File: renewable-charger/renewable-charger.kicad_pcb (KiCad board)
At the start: 0 parts

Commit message: Schematic almost finished—most components chosen with part numbers.  Start made on PCB.  Part of #2
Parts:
- added BT1: Battery_Cell, Connector_JST:JST_PH_S2B-PH-SM4-TB_1x02-1MP_P2.00mm_Horizontal, F.Cu at (158.8, 71.1)
- added C1: 1uF, Capacitor_SMD:C_0603_1608Metric_Pad1.08x0.95mm_HandSolder, F.Cu at (142.9, 73.7)
- added C2: 0.1uF, Capacitor_SMD:C_0603_1608Metric_Pad1.08x0.95mm_HandSolder, F.Cu at (75.6, 89.5)
- added C3: 1uF, Capacitor_SMD:C_0603_1608Metric_Pad1.08x0.95mm_HandSolder, F.Cu at (99.7, 69.2)
- added C4: 220nF, Capacitor_SMD:C_0603_1608Metric_Pad1.08x0.95mm_HandSolder, F.Cu at (137.2, 83.2)
- added C6: 10uF 50V, Capacitor_SMD:C_1206_3216Metric_Pad1.33x1.80mm_HandSolder, F.Cu at (92.1, 59.7)
- added C7: 10uF 50V, Capacitor_SMD:C_1206_3216Metric_Pad1.33x1.80mm_HandSolder, F.Cu at (99.7, 65.4)
- added D1: D_Zener, Diode_SMD:D_SMF, F.Cu at (114.9, 48.9)
- added D2: D_Zener, Diode_SMD:D_SMF, F.Cu at (106.7, 48.9)
- added D3: LED Green, LED_SMD:LED_0805_2012Metric_Pad1.15x1.40mm_HandSolder, F.Cu at (64.8, 76.8)
- added D4: LED Red, LED_SMD:LED_0805_2012Metric_Pad1.15x1.40mm_HandSolder, F.Cu at (64.8, 71.1)
- added L1: 100uH 2.5A, Inductor_SMD:L_12x12mm_H6mm, F.Cu at (74.3, 54.0)
- added Q1: P-channel 30V 4A MOSfet, Package_TO_SOT_SMD:SOT-23, F.Cu at (124.5, 52.1)
- added R1: R_Small, Resistor_SMD:R_0603_1608Metric_Pad0.98x0.95mm_HandSolder, F.Cu at (54.0, 74.9)
- added R2: 120R, Resistor_SMD:R_0603_1608Metric_Pad0.98x0.95mm_HandSolder, F.Cu at (120.0, 84.5)
- added R3: R_Small, Resistor_SMD:R_0805_2012Metric_Pad1.20x1.40mm_HandSolder, F.Cu at (104.1, 92.7)
- added R4: R_Small, Resistor_SMD:R_0805_2012Metric_Pad1.20x1.40mm_HandSolder, F.Cu at (111.8, 90.8)
- added R5: Rcs, Resistor_SMD:R_0805_2012Metric_Pad1.20x1.40mm_HandSolder, F.Cu at (137.4, 60.3)
- added U1: CN3791, Package_SO:SSOP-10_3.9x4.9mm_P1.00mm, F.Cu at (84.3, 76.0)
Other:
- copper layers 0 -> 2

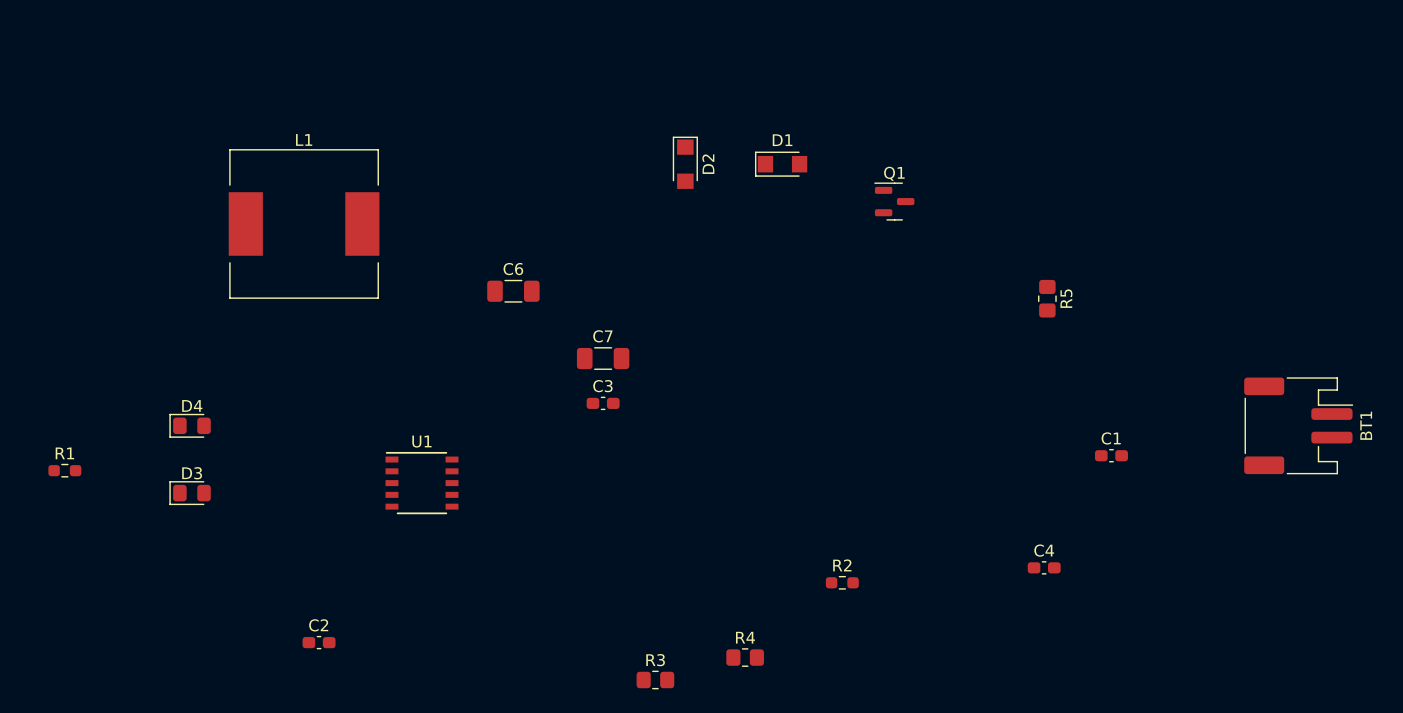
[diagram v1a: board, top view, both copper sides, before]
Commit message: Add windmill rectifying voltage-doubler circuit to the schematic.  Part of #6
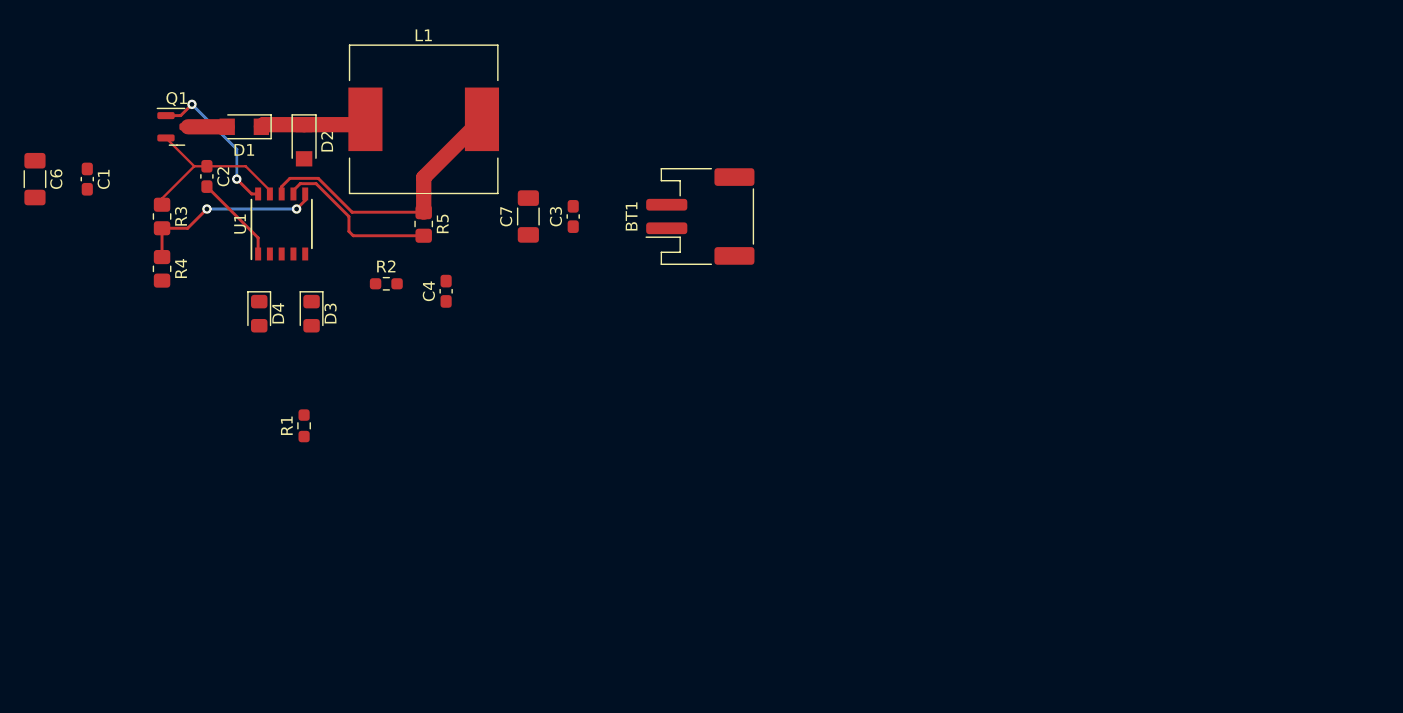
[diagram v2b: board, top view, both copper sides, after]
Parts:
- moved C1 90.1 mm to (55.9, 50.2), turned to -90 degrees
- moved Q1 61.3 mm to (63.5, 45.7)
- moved R4 59.5 mm to (62.2, 57.8), turned to -90 degrees
- moved R3 57.5 mm to (62.2, 53.3), turned to -90 degrees
- moved C4 56.0 mm to (86.4, 59.7), turned to 90 degrees
- moved BT1 53.8 mm to (108.0, 53.3), turned to 90 degrees
- moved R5 53.4 mm to (84.5, 54.0)
- moved R2 46.3 mm to (81.3, 59.1)
- moved D1 45.8 mm to (69.2, 45.7), turned to 180 degrees
- moved C6 41.7 mm to (51.4, 50.2), turned to -90 degrees
- moved C2 40.7 mm to (66.0, 49.9), turned to -90 degrees
- moved D2 32.4 mm to (74.3, 47.0)
- moved U1 25.0 mm to (72.4, 54.0), turned to 90 degrees
- moved R1 20.7 mm to (74.3, 71.1), turned to 90 degrees
- moved D3 18.3 mm to (74.9, 61.6), turned to -90 degrees
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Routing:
- net Net-(U1-CSP): track 0.00 -> 24.1 mm
- net Net-(U1-MPPT): track 0.00 -> 16.1 mm, vias 0 -> 2
- net /Power +: track 0.00 -> 15.4 mm
- net Net-(BT1-+): track 0.00 -> 14.2 mm
- net Net-(Q1-G): track 0.00 -> 12.9 mm, vias 0 -> 2
- net Net-(D1-K): track 0.00 -> 9.10 mm
- net Net-(U1-VG): track 0.00 -> 7.53 mm
- net Net-(D1-A): track 0.00 -> 3.33 mm

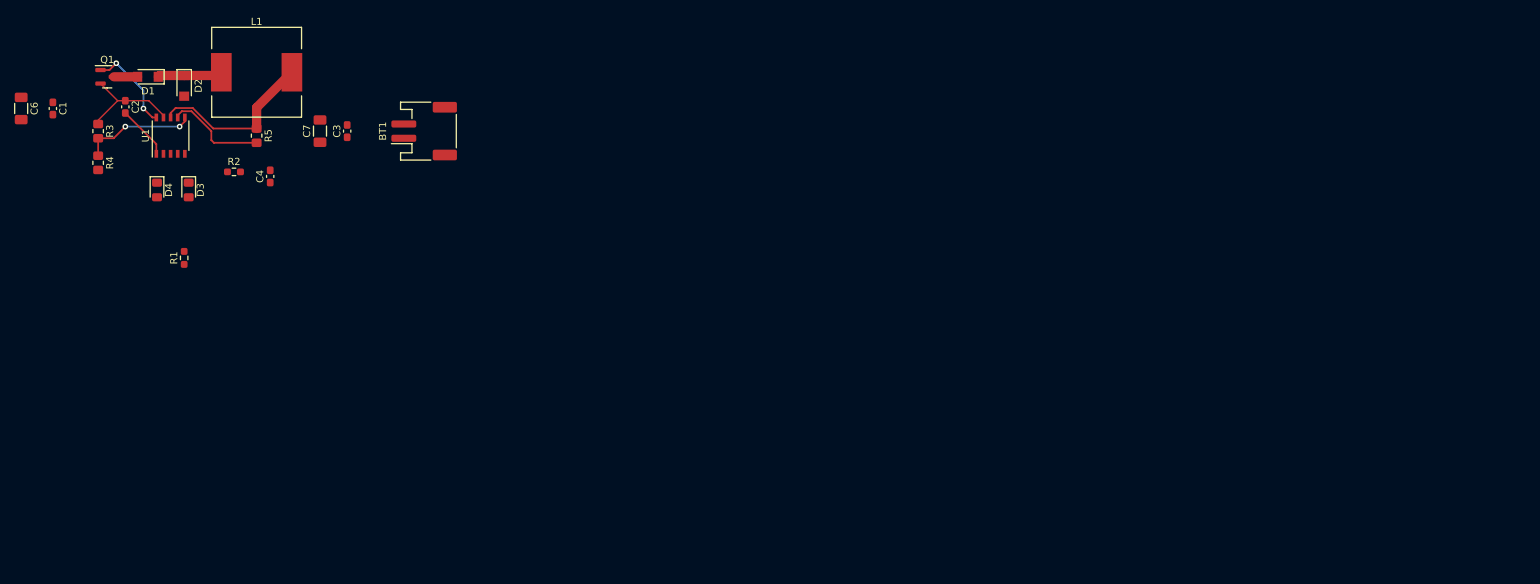
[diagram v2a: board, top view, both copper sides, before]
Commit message: The windmill rectifier circuit is laid out on the PCB, apart from routing bits to the output connector, as its final location isn't set yet.  Part of #6
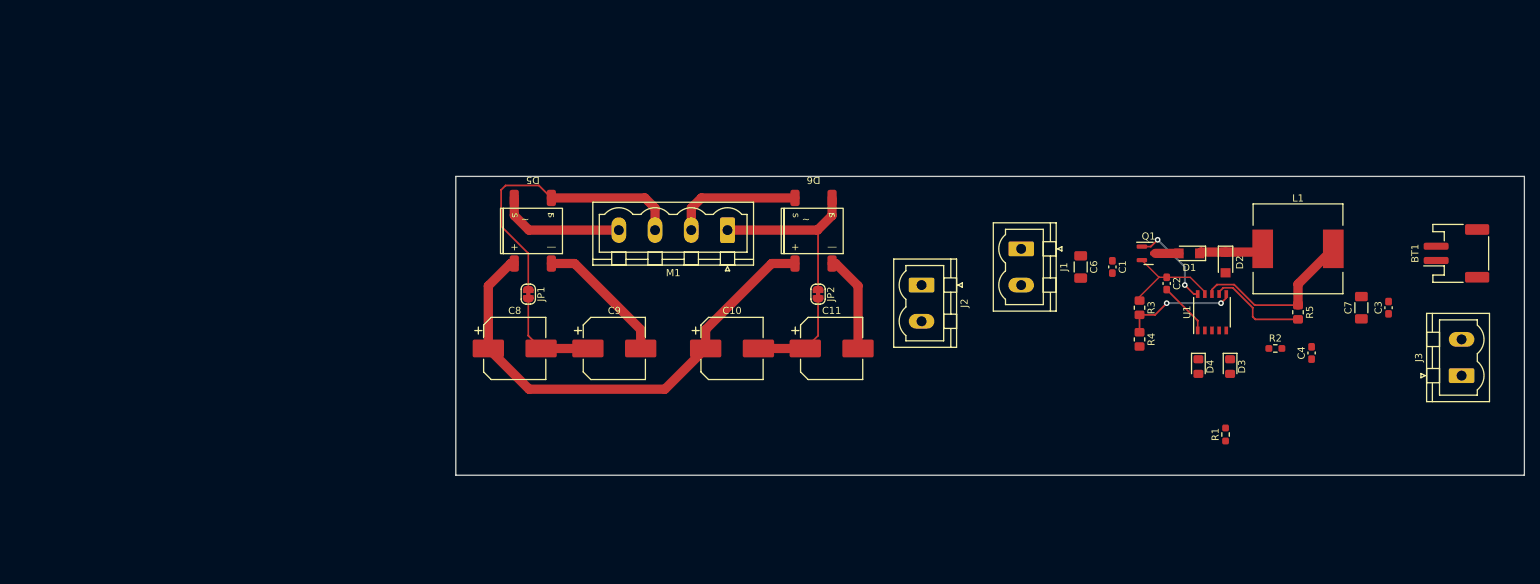
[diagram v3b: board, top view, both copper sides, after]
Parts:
- added C10: C_Polarized_Small, Capacitor_SMD:CP_Elec_8x10.5, F.Cu at (151.1, 83.8)
- added C11: C_Polarized_Small, Capacitor_SMD:CP_Elec_8x10.5, F.Cu at (165.1, 83.8)
- added C8: C_Polarized_Small, Capacitor_SMD:CP_Elec_8x10.5, F.Cu at (120.7, 83.8)
- added C9: C_Polarized_Small, Capacitor_SMD:CP_Elec_8x10.5, F.Cu at (134.6, 83.8)
- added D5: D_Bridge_+-AA, BridgeRectifier:BridgeRectifier_DBLS, F.Cu at (123.2, 67.3)
- added D6: D_Bridge_+-AA, BridgeRectifier:BridgeRectifier_DBLS, F.Cu at (162.6, 67.3)
- added J1: Solar Input, Connector_Phoenix_MSTB:PhoenixContact_MSTBVA_2,5_2-G-5,08_1x02_P5.08mm_Vertical, F.Cu at (191.7, 69.8)
- added J2: Wind Output, Connector_Phoenix_MSTB:PhoenixContact_MSTBVA_2,5_2-G-5,08_1x02_P5.08mm_Vertical, F.Cu at (177.7, 74.9)
- added J3: Output, Connector_Phoenix_MSTB:PhoenixContact_MSTBVA_2,5_2-G-5,08_1x02_P5.08mm_Vertical, F.Cu at (253.5, 87.6)
- added JP1: SolderJumper_2_Bridged, Jumper:SolderJumper-2_P1.3mm_Bridged_RoundedPad1.0x1.5mm, F.Cu at (122.6, 76.2)
- added JP2: SolderJumper_2_Bridged, Jumper:SolderJumper-2_P1.3mm_Bridged_RoundedPad1.0x1.5mm, F.Cu at (163.2, 76.2)
- added M1: Stepper_Motor_bipolar, Connector_Phoenix_MSTB:PhoenixContact_MSTBVA_2,5_4-G-5,08_1x04_P5.08mm_Vertical, F.Cu at (150.5, 67.2)
- moved C1 150.2 mm to (204.5, 72.4)
- moved C6 150.2 mm to (200.0, 72.4)
- moved C2 148.1 mm to (212.1, 74.7)
- moved C3 148.1 mm to (243.2, 78.1)
- moved C4 148.1 mm to (232.4, 84.5)
- moved C7 148.1 mm to (239.4, 78.1)
- moved D2 148.1 mm to (220.3, 71.8)
- moved D4 148.1 mm to (216.5, 86.4)
- moved L1 148.1 mm to (230.5, 69.8)
- moved Q1 148.1 mm to (209.6, 70.5)
- moved R1 148.1 mm to (220.3, 95.9)
- moved R2 148.1 mm to (227.3, 83.8)
- moved R3 148.1 mm to (208.3, 78.1)
- moved R4 148.1 mm to (208.3, 82.5)
- moved R5 148.1 mm to (230.5, 78.7)
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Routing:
- net /Power +: track 15.4 -> 83.4 mm
- net Net-(JP1-A): track 0.00 -> 41.8 mm
- net /Power -: track 0.00 -> 32.7 mm
- net Net-(JP2-A): track 0.00 -> 26.3 mm
- net Net-(M1--): track 0.00 -> 18.2 mm
- net Net-(D5-Pad3): track 0.00 -> 18.0 mm
- net Net-(JP2-B): track 0.00 -> 14.3 mm
- net Net-(JP1-B): track 0.00 -> 14.3 mm
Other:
- board outline added: 149.9 x 41.9 mm
